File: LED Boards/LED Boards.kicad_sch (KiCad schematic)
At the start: 21 parts, among them J1 Conn_01x02, J2 Conn_01x05, J3 USB_C_Receptacle_PowerOnly_6P, Q1 RS9N50D, U1 NSL-32, U2 AMC1301DWVR

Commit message: heliospherev1.4
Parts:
- removed C1, C4: 10nF, symbol Device:C
- removed C2: 0.1 uF, symbol Device:C
- removed C3: 10 uF, symbol Device:C
- removed J2: Conn_01x05, symbol Connector_Generic:Conn_01x05
- removed J3: USB_C_Receptacle_PowerOnly_6P, symbol Connector:USB_C_Receptacle_PowerOnly_6P
- removed Q1: RS9N50D, Package_TO_SOT_SMD:TO-252-2, symbol Transistor_FET:RS9N50D
- removed R1: 40, Resistor_SMD:R_1812_4532Metric_Pad1.30x3.40mm_HandSolder, symbol Device:R
- removed R2: 10k, Resistor_SMD:R_1812_4532Metric_Pad1.30x3.40mm_HandSolder, symbol Device:R
- removed R4, R5, R7, R8: 10, Resistor_SMD:R_1812_4532Metric_Pad1.30x3.40mm_HandSolder, symbol Device:R
- removed RSHUNT1: 0.1, Resistor_SMD:R_1812_4532Metric_Pad1.30x3.40mm_HandSolder, symbol Device:R
- removed U1: NSL-32, OptoDevice:Luna_NSL-32, symbol Isolator:NSL-32
- removed U2: AMC1301DWVR, AMC1301DWVR:SOIC127P1150X280-8N, symbol AMC1301:AMC1301DWVR
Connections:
- net GND: now also D2.1 (K)
- no-connect marks 2 -> 0
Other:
- note removed: "+3V3 from computer"
- note removed: "Connect to power supply, which is set to 75 V 1 A"
- note removed: "Voltage differential from op amp is sent to MCU"
- moved on the sheet: J1

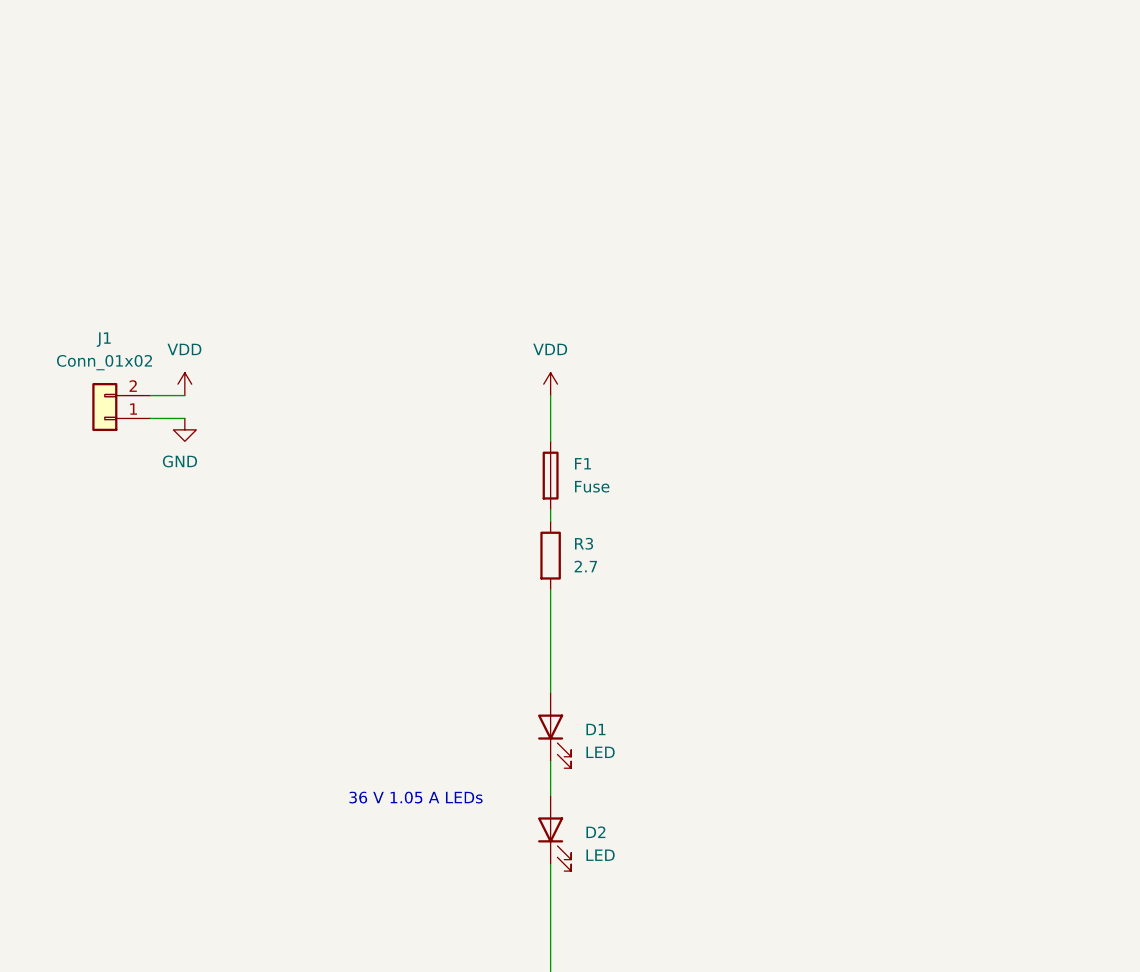
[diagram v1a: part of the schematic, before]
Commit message: Centralized isolation amp power source. Corrected STM32 pins.
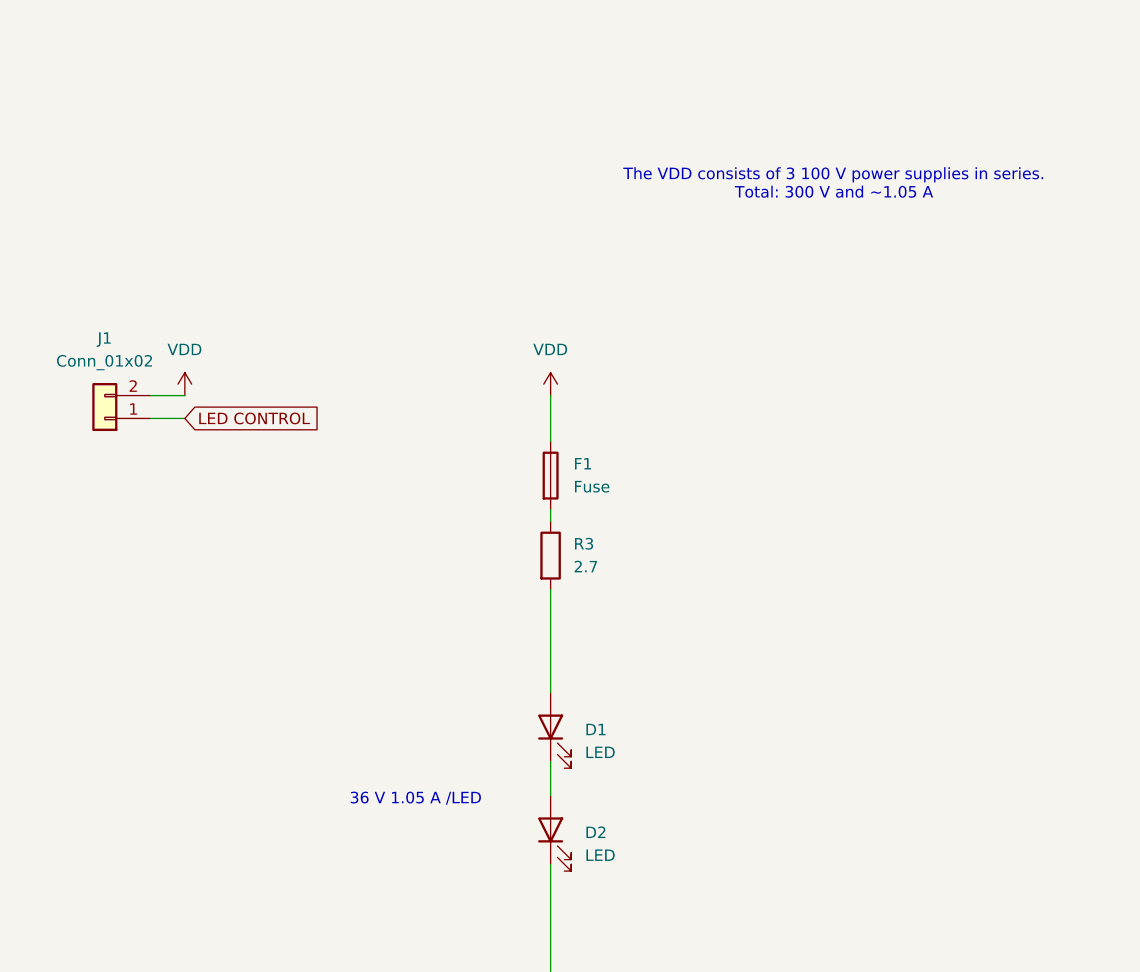
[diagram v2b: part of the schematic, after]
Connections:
- net GND: no longer J1.1 (Pin_1)
- new net LED CONTROL: J1.1 (Pin_1)
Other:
- note added: "36 V 1.05 A /LED"
- note added: "The VDD consists of 3 100 V power supplies in series. Total: 300 V and ~1.05 A"
- note removed: "36 V 1.05 A LEDs"
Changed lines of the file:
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@@
 		)
 	)
-	(text "36 V 1.05 A LEDs"
+	(text "36 V 1.05 A /LED"
 		(exclude_from_sim no)
 		(at 119.634 104.648 0)
@@
 		)
 	)
+	(text "The VDD consists of 3 100 V power supplies in series. \nTotal: 300 V and ~1.05 A"
+		(exclude_from_sim no)
+		(at 166.116 36.322 0)
+		(effects
+			(font
+				(size 1.27 1.27)
+			)
+		)
+	)
 	(text_box "VVD uses the IKOKKO 100 V Power Supply (can supply up to 3 A, 120 V)"
 		(exclude_from_sim no)
@@
 			(width 0)
 			(type default)
+		)
+	)
+	(global_label "LED CONTROL"
+		(shape input)
+		(at 93.98 62.23 0)
+		(fields_autoplaced yes)
+		(effects
+			(font
+				(size 1.27 1.27)
+			)
+			(justify left)
+		)
+		(property "Intersheetrefs" "${INTERSHEET_REFS}"
+			(at 109.9071 62.23 0)
+			(effects
+				(font
+					(size 1.27 1.27)
+				)
+				(justify left)
+				(hide yes)
+			)
 		)
 	)
@@
 					(unit 1)
 				)
-			)
-		)
-	)
-	(symbol
-		(lib_id "power:GND")
-		(at 93.98 62.23 0)
-		(unit 1)
-		(exclude_from_sim no)
-		(in_bom yes)
-		(on_board yes)
-		(dnp no)
-		(property "Reference" "#PWR017"
-			(at 93.98 68.58 0)
-			(effects
-				(font
-					(size 1.27 1.27)
-				)
-				(hide yes)
-			)
-		)
-		(property "Value" "GND"
-			(at 91.44 67.056 0)
-			(effects
-				(font
-					(size 1.27 1.27)
-				)
-				(justify left)
-			)
-		)
-		(property "Footprint" ""
-			(at 93.98 62.23 0)
-			(effects
-				(font
-					(size 1.27 1.27)
-				)
-				(hide yes)
-			)
-		)
-		(property "Datasheet" ""
-			(at 93.98 62.23 0)
-			(effects
-				(font
-					(size 1.27 1.27)
-				)
-				(hide yes)
-			)
-		)
-		(property "Description" "Power symbol creates a global label with name \"GND\" , ground"
-			(at 93.98 62.23 0)
-			(effects
-				(font
-					(size 1.27 1.27)
-				)
-				(hide yes)
-			)
-		)
-		(pin "1"
-		)
-		(instances
-			(project "LED Boards"
-				(path "/e372ef32-cef9-49e1-9c36-c69f7dac307f"
-					(reference "#PWR017")
-					(unit 1)
-				)
